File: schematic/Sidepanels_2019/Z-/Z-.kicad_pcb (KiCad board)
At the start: 2 copper layers, 98 x 70.5 mm, 5 parts, among them J1 Conn_01x04, J2 Conn_01x02

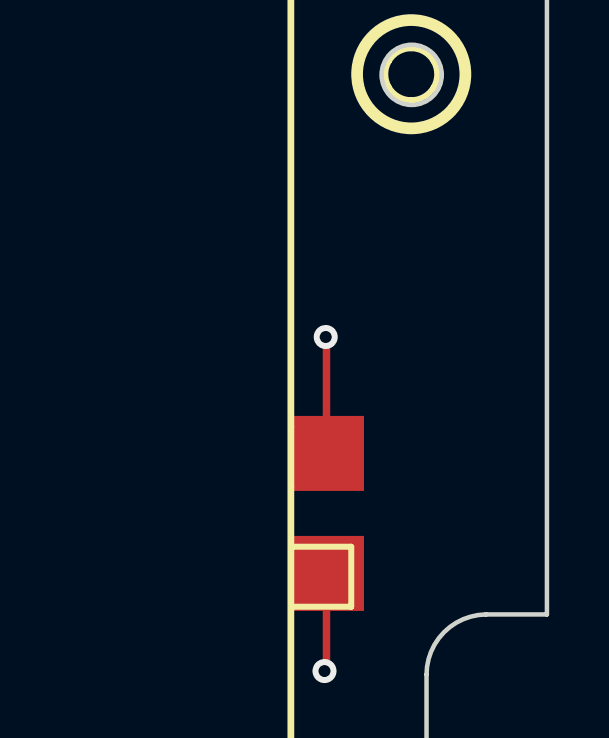
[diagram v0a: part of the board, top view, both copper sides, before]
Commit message: Update to all boards
Added labels to boards to resolve issue #2
Added names of students and faculty to boards
Generated Step files to resolve issue #4, please note the export does include the silkscreen.
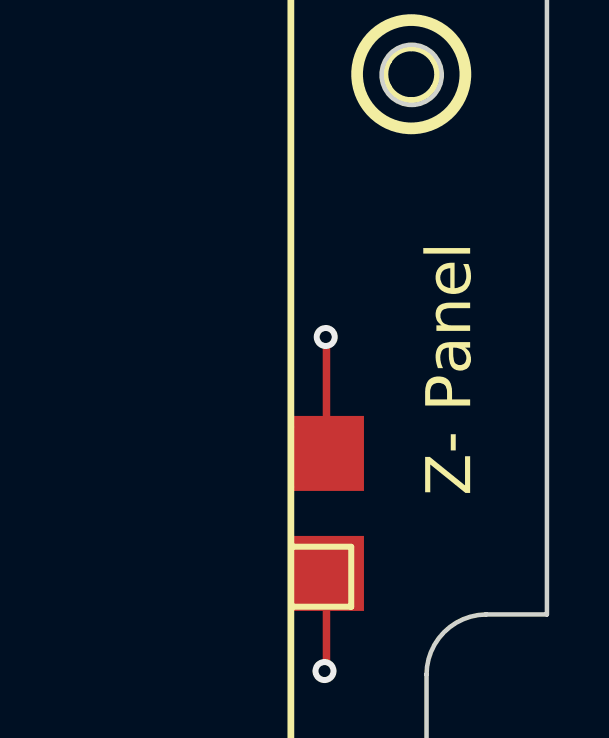
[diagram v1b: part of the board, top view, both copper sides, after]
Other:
- board text added: "Z- Panel"

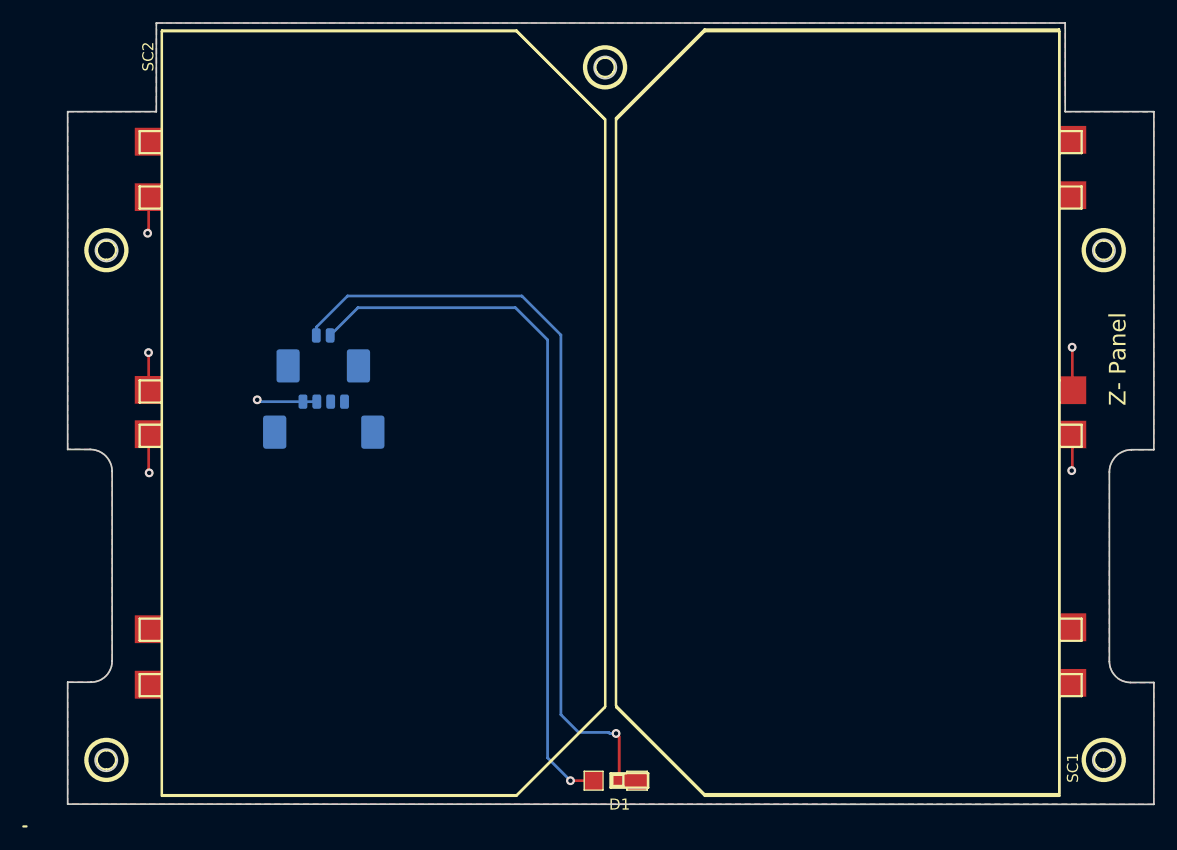
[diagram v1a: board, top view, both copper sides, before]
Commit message: Push of all changes made for June update
Major change was in the solar cell and creating a new library based on the old one.
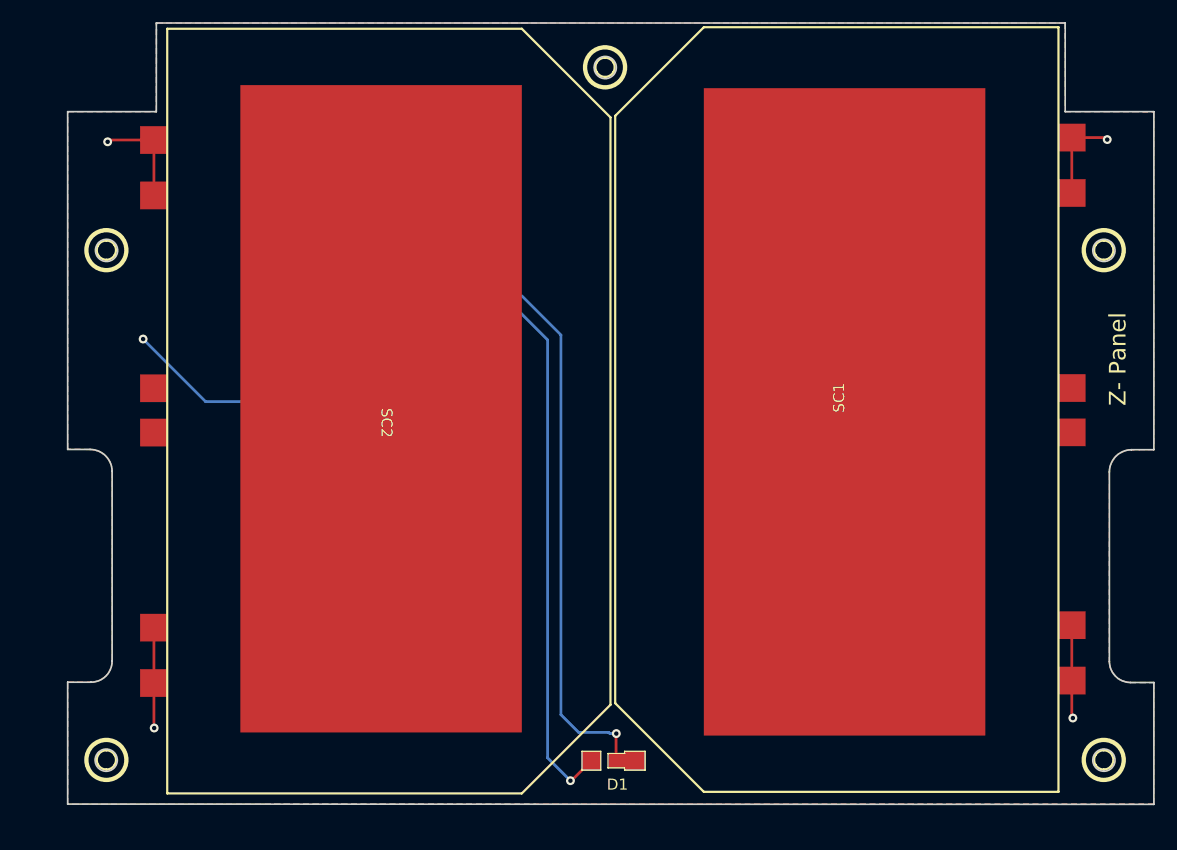
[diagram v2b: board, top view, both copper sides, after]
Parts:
- SC1, SC2: footprint CySat footprints:Spectrolab -> CySat:Spectrolabs_UTJ
- moved SC2 22.4 mm to (119.6, 83.9)
- moved SC1 22.0 mm to (161.4, 81.6)
- moved D1 1.81 mm to (140.9, 114.3)
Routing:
- net VSS: track 14.0 -> 35.0 mm
- net VCC: track 8.75 -> 18.0 mm, vias 2 -> 1
- net Net-(D1-Pad1): track 71.4 -> 67.9 mm
- net Net-(D1-Pad2): track 64.6 -> 65.1 mm
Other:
- net class Default removed
- rule pad_to_mask_clearance: 0.051 -> 0
